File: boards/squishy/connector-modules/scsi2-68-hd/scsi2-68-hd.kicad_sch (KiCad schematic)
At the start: 14 parts, among them J1 SCSI PHY Mezz, J2 Conn_02x25_Odd_Even, J3 Conn_01x04, J4 Conn_02x34_Clockwise_Shield, J5 Conn_02x24_Clockwise_Shield, U1 M24C02-RMC

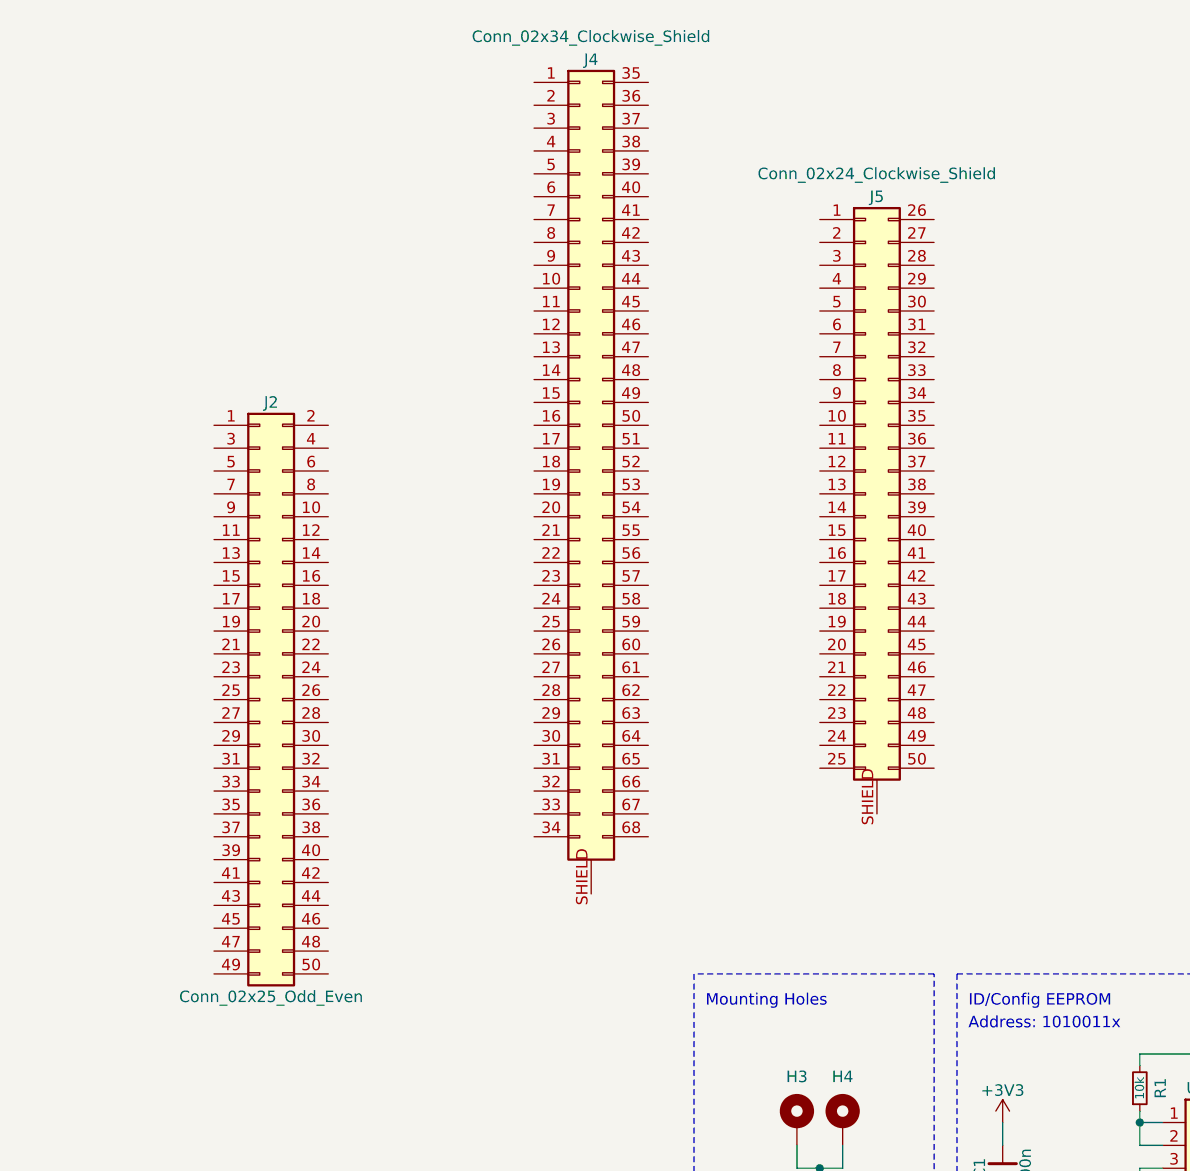
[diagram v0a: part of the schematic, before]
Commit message: squishy: connectors: Removed unneeded connector symbols in the given kicad schematics
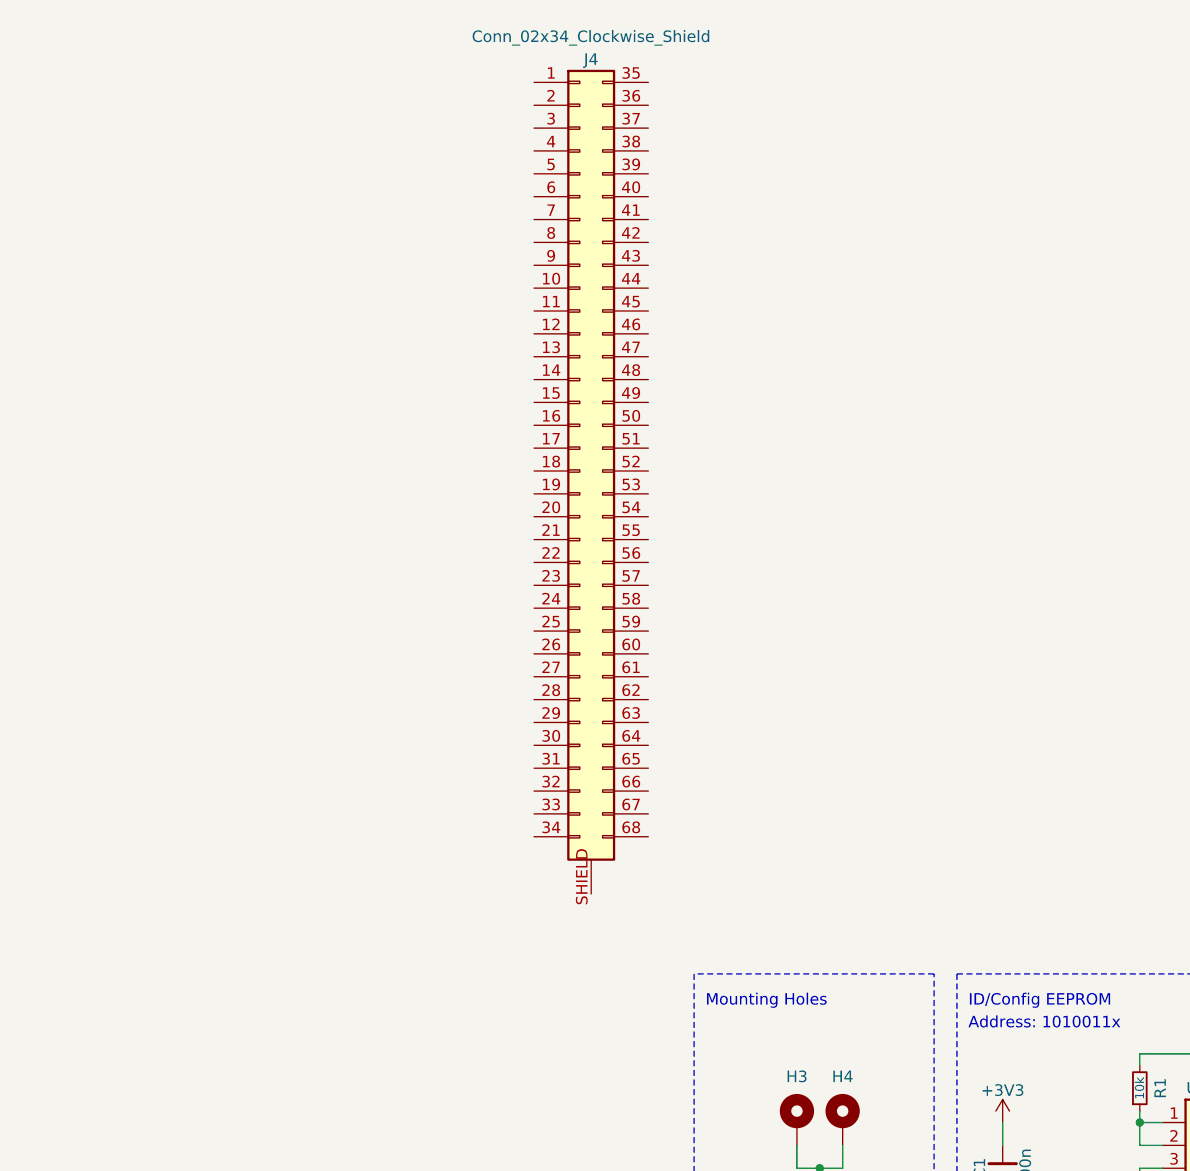
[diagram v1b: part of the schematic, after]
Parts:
- removed J2: Conn_02x25_Odd_Even, Connector_IDC:IDC-Header_2x25_P2.54mm_Horizontal, symbol Connector_Generic:Conn_02x25_Odd_Even
- removed J5: Conn_02x24_Clockwise_Shield, symbol lethalbit-connectors:Conn_02x25_Counter_Clockwise

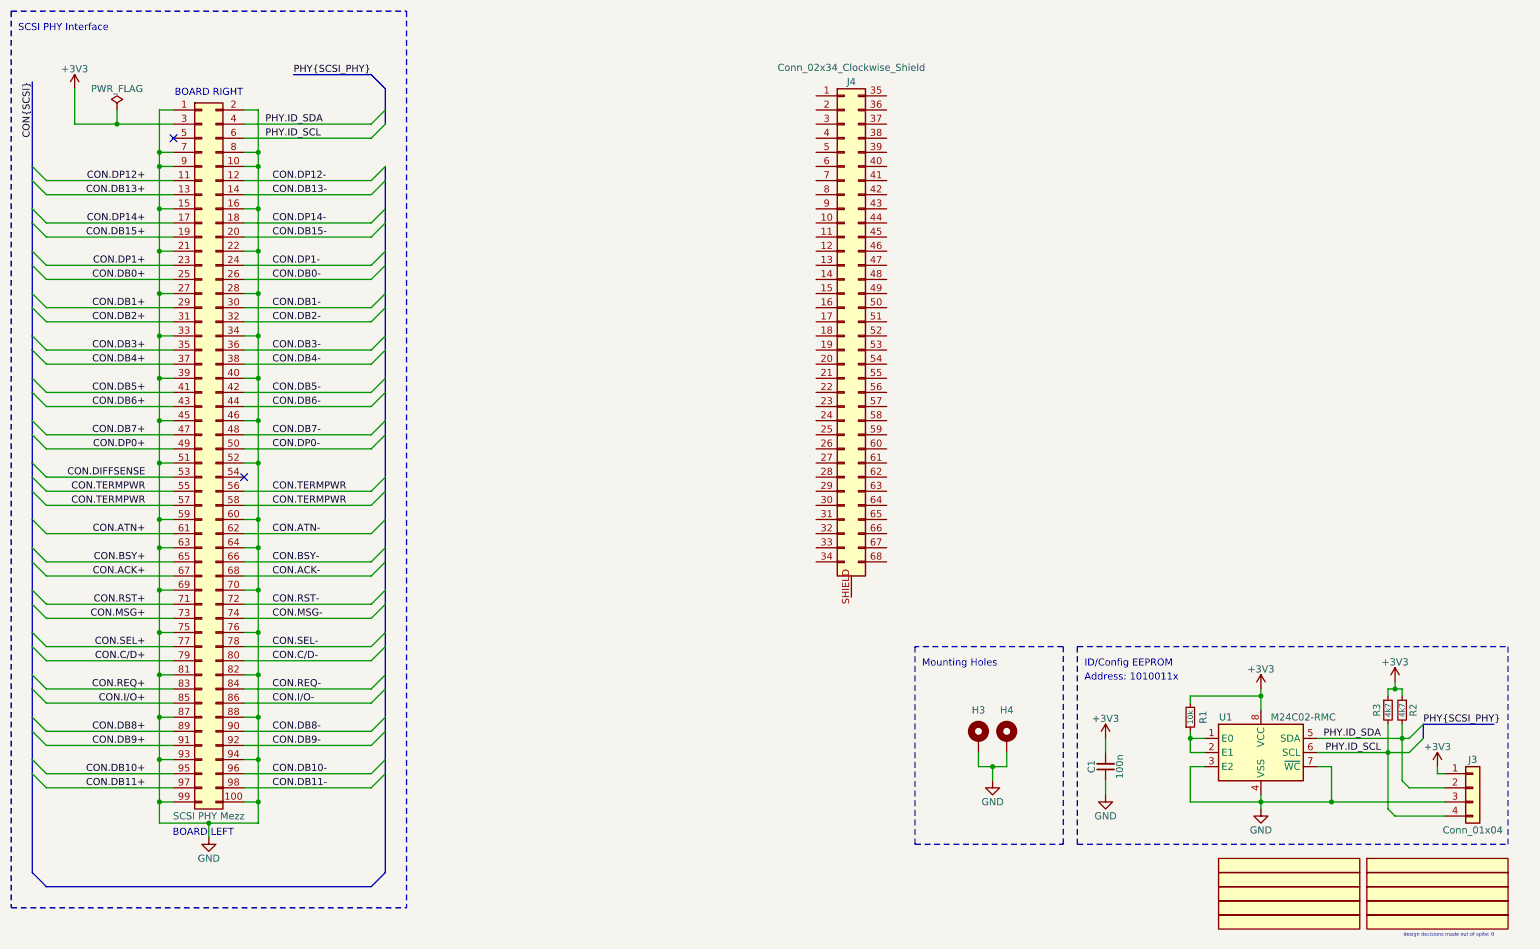
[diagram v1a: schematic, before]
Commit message: squishy: connectors: Cleaned up and unified look/feel of connector schematics
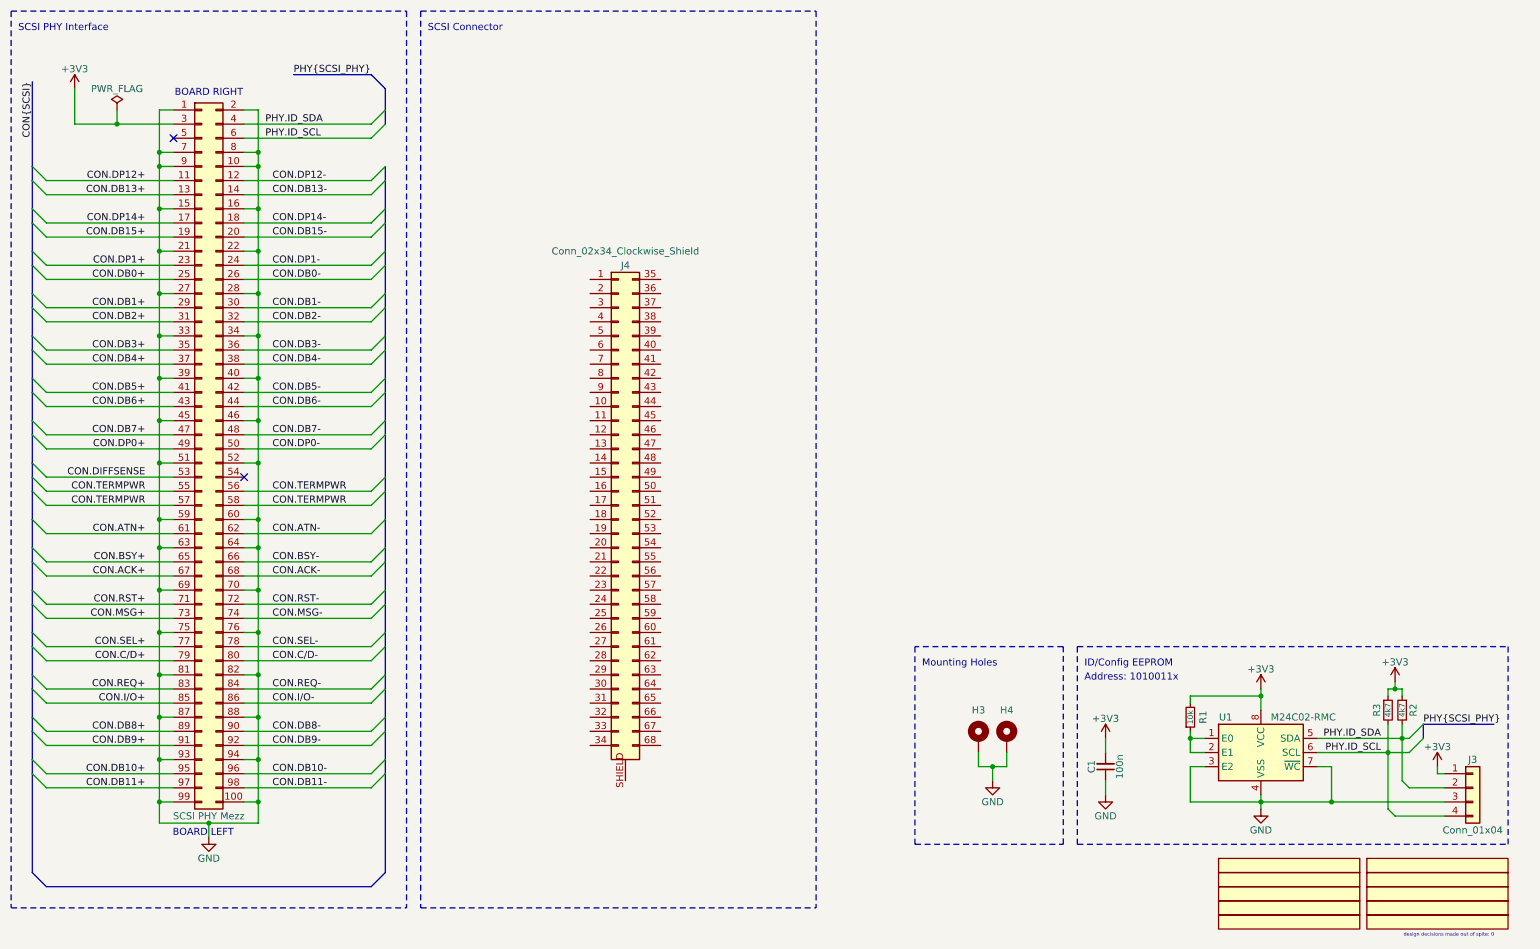
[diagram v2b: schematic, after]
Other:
- note added: "SCSI Connector"
- moved on the sheet: J4
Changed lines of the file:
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@@
+		)
+	)
+	(polyline
+		(pts
+			(xy 87.63 175.26) (xy 158.75 175.26)
+		)
+		(stroke
+			(width 0)
+			(type dash)
 		)
 	)
@@
 		)
 	)
+	(polyline
+		(pts
+			(xy 87.63 13.97) (xy 87.63 175.26)
+		)
+		(stroke
+			(width 0)
+			(type dash)
+		)
+	)
 	(bus
 		(pts
@@
 		)
 	)
+	(polyline
+		(pts
+			(xy 87.63 13.97) (xy 158.75 13.97)
+		)
+		(stroke
+			(width 0)
+			(type dash)
+		)
+	)
 	(bus
 		(pts
@@
 			(width 0)
 			(type default)
+		)
+	)
+	(polyline
+		(pts
+			(xy 158.75 13.97) (xy 158.75 175.26)
+		)
+		(stroke
+			(width 0)
+			(type dash)
 		)
 	)
@@
 				(size 1.27 1.27)
 			)
+		)
+	)
+	(text "SCSI Connector"
+		(exclude_from_sim no)
+		(at 88.9 17.78 0)
+		(effects
+			(font
+				(size 1.27 1.27)
+			)
+			(justify left bottom)
 		)
 	)
@@
 	(symbol
 		(lib_id "lethalbit-connectors:Conn_02x34_Counter_Clockwise")
-		(at 165.1 69.85 0)
+		(at 124.46 102.87 0)
 		(unit 1)
 		(exclude_from_sim no)
@@
 		(dnp no)
 		(property "Reference" "J4"
-			(at 165.1 26.67 0)
+			(at 124.46 59.69 0)
 			(effects
 				(font
@@
 		)
 		(property "Value" "Conn_02x34_Clockwise_Shield"
-			(at 165.1 24.13 0)
+			(at 124.46 57.15 0)
 			(effects
 				(font
@@
 		)
 		(property "Footprint" ""
-			(at 163.83 77.47 0)
+			(at 123.19 110.49 0)
 			(effects
 				(font
@@
 		)
 		(property "Datasheet" "~"
-			(at 163.83 77.47 0)
+			(at 123.19 110.49 0)
 			(effects
 				(font
@@
 		)
 		(property "Description" "Generic connector, double row, 02x34 counter clockwise pin numbering scheme (similar to DIP package numbering), with shielding"
-			(at 165.1 69.596 0)
-			(effects
-				(font
+			(at 124.46 102.616 0)
+			(effects
+				(font

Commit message: squishy: connectors: updated schematic title blocks for connectors as appropriate
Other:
- title: Squishy -  ICD 50 -> Squishy -  SCSI-2 VHDCI Connector Module
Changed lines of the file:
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@@
 	(paper "A4")
 	(title_block
-		(title "Squishy -  ICD 50")
-		(date "2024-08-22")
+		(title "Squishy -  SCSI-2 VHDCI Connector Module")
+		(date "2024-09-17")
 		(rev "1")
 		(company "Shrine Maiden Heavy Industries")

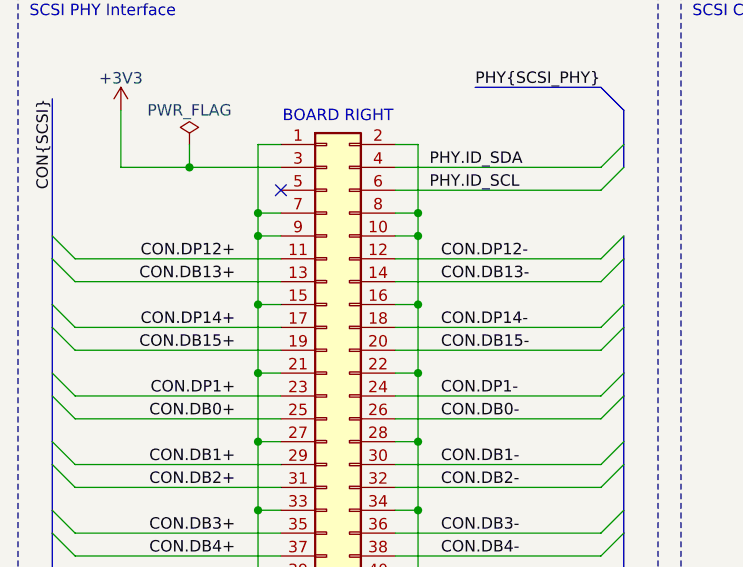
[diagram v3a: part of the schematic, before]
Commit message: squishy: connectors: s/DP12/DB12/g s/DP14/DB14/g
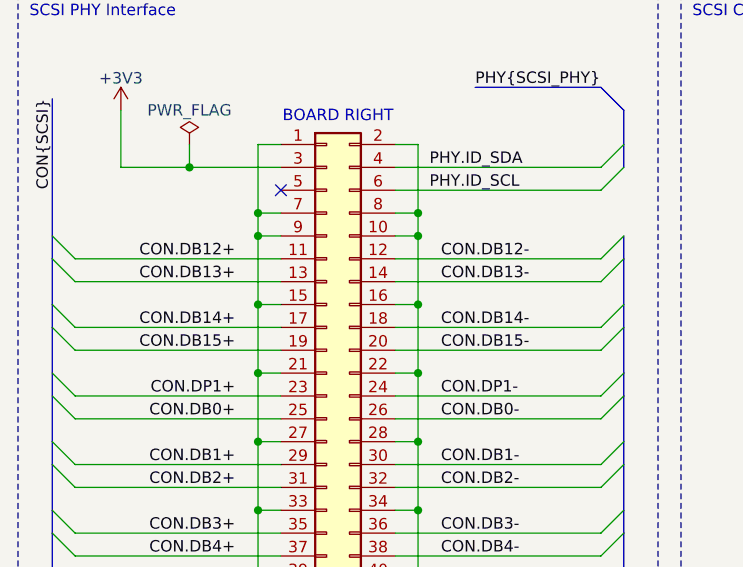
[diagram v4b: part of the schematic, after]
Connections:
- net CON.DP12+ renamed CON.DB12+
- net CON.DP12- renamed CON.DB12-
- net CON.DP14+ renamed CON.DB14+
- net CON.DP14- renamed CON.DB14-
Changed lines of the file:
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@@
 		)
 	)
-	(label "CON.DP14-"
+	(label "CON.DB14-"
 		(at 60.96 52.07 0)
 		(fields_autoplaced yes)
@@
 		)
 	)
-	(label "CON.DP12+"
+	(label "CON.DB12+"
 		(at 38.1 44.45 180)
 		(fields_autoplaced yes)
@@
 		)
 	)
-	(label "CON.DP12-"
+	(label "CON.DB12-"
 		(at 60.96 44.45 0)
 		(fields_autoplaced yes)
@@
 		)
 	)
-	(label "CON.DP14+"
+	(label "CON.DB14+"
 		(at 38.1 52.07 180)
 		(fields_autoplaced yes)
